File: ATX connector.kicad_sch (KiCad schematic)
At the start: 15 parts, among them J400 15246040, J402 ATX-24

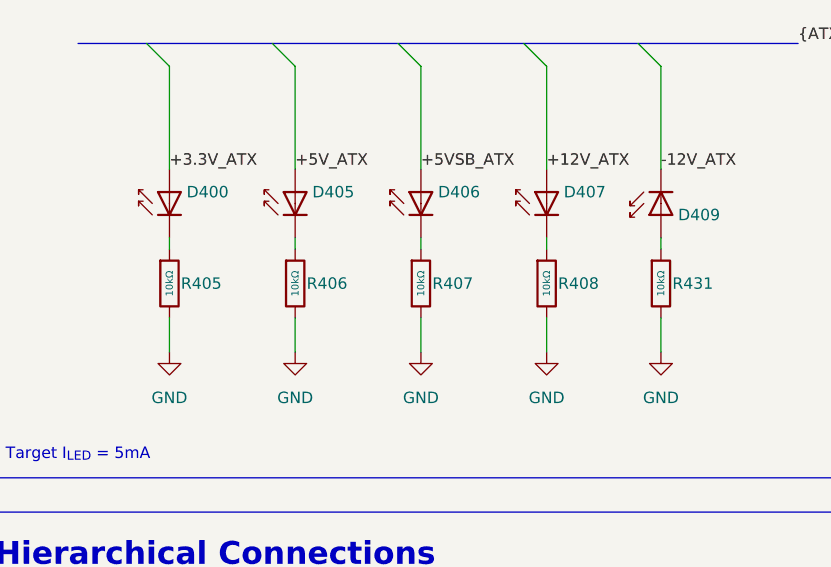
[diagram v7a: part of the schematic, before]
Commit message: updated LED resistor values
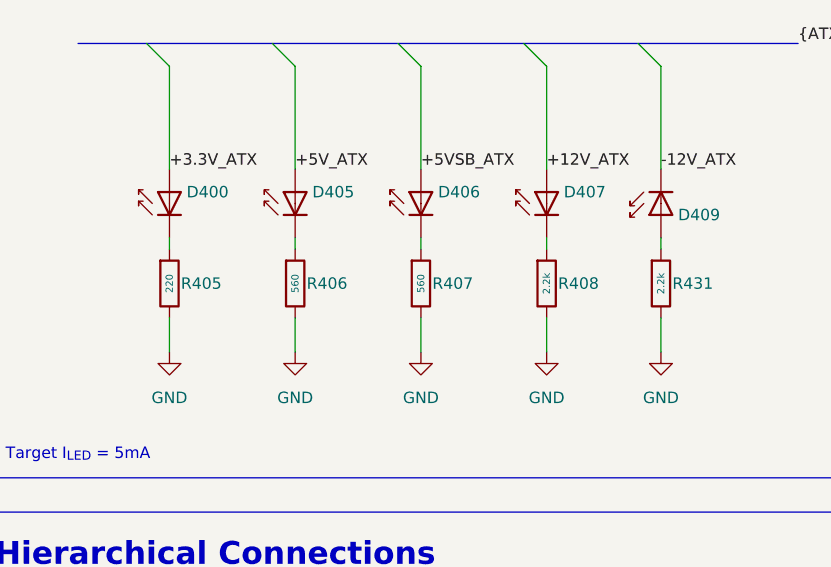
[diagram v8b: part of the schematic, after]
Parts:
- R405: value 10kΩ -> 220
- R406, R407: value 10kΩ -> 560
- R408, R431: value 10kΩ -> 2.2k
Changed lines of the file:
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@@
 			)
 		)
-		(property "Value" "10kΩ"
+		(property "Value" "2.2k"
 			(at 251.46 62.23 90)
 			(do_not_autoplace yes)
@@
 			)
 		)
-		(property "Value" "10kΩ"
+		(property "Value" "560"
 			(at 210.82 62.23 90)
 			(do_not_autoplace yes)
@@
 			)
 		)
-		(property "Value" "10kΩ"
+		(property "Value" "560"
 			(at 224.79 62.23 90)
 			(do_not_autoplace yes)
@@
 			)
 		)
-		(property "Value" "10kΩ"
+		(property "Value" "220"
 			(at 196.85 62.23 90)
 			(do_not_autoplace yes)
@@
 			)
 		)
-		(property "Value" "10kΩ"
+		(property "Value" "2.2k"
 			(at 238.76 62.23 90)
 			(do_not_autoplace yes)
